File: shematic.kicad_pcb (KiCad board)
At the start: 2 copper layers, 90 x 50.8 mm, 73 parts, among them J1 VIN, J10 SRESU, J11 RESET, J12 Conn_02x03_Odd_Even, J13 Conn_02x03_Odd_Even, J14 Conn_02x03_Odd_Even, J15 X, J16 Y, J17 Z, J2 COOL_ENB, J3 SP/LAS, J4 PROBE, J5 LIM_X, J6 LIM_Y, J7 LIM_Z, J8 ESTOP, J9 FHOLD, U1 4050, U2 MC34063AD, U3 AZ1117-5.0, U4 PC817

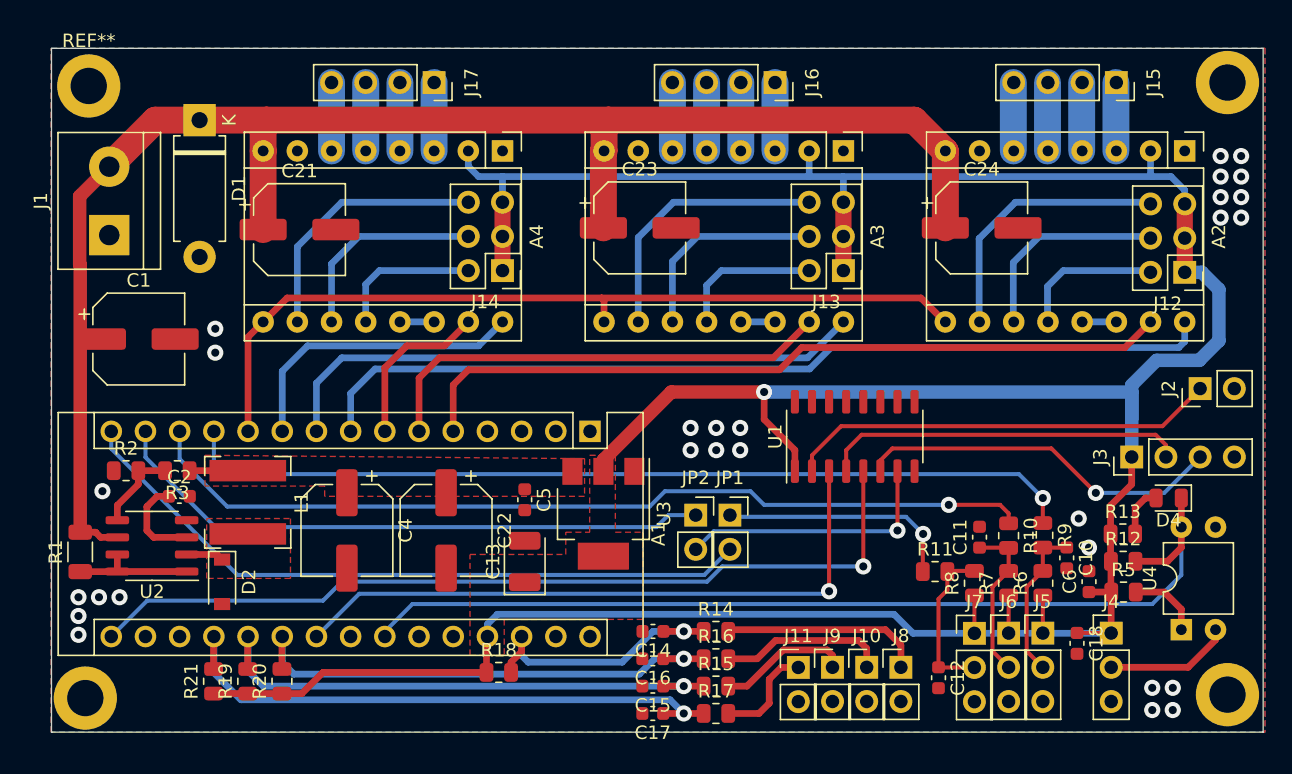
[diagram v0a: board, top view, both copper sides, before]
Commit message: replaced footprints for passive component, edited silkscreens
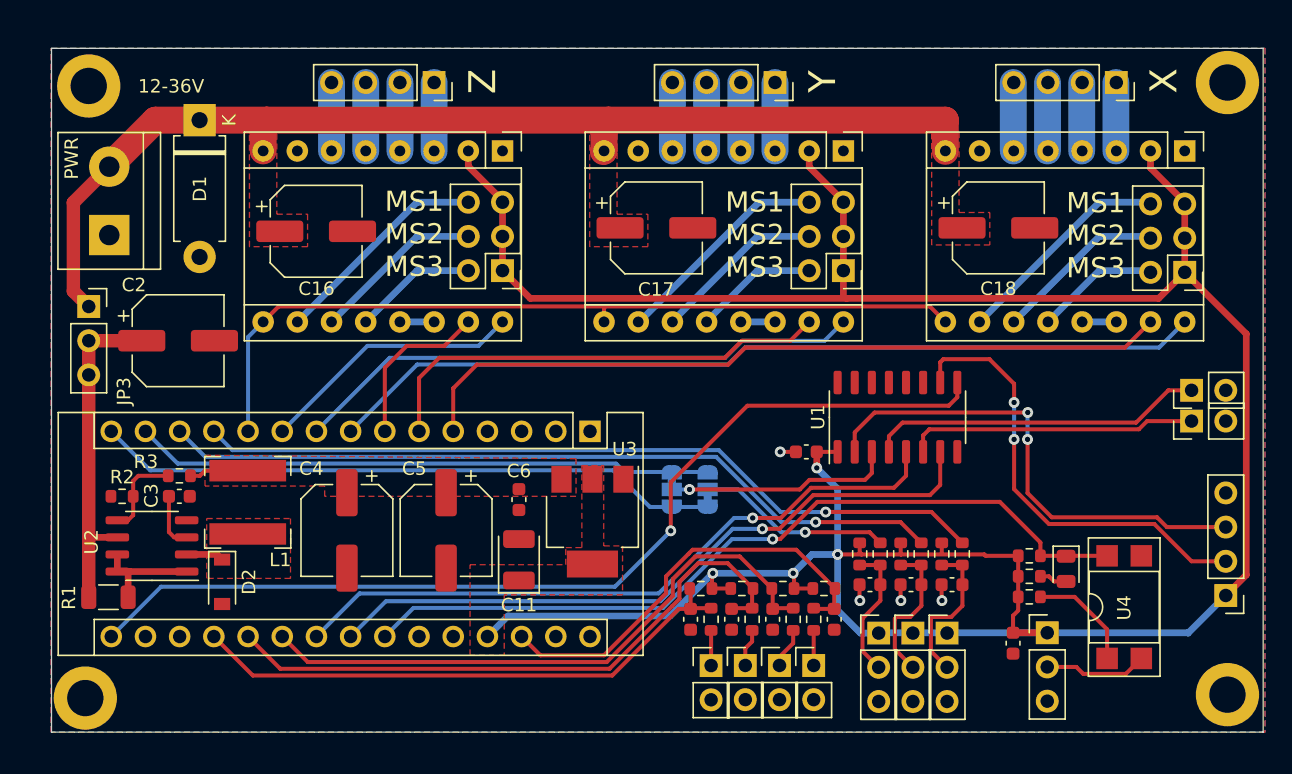
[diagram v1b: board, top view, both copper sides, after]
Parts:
- removed the C18 at (106.2, 73.4)
- added C1: 100n, Capacitor_SMD:C_0603_1608Metric, F.Cu at (86.1, 59.2)
- added J3: COOL_ENB, Connector_PinHeader_2.54mm:PinHeader_1x02_P2.54mm_Vertical, F.Cu at (114.7, 54.6)
- added JP3: EXT_PWR, Connector_PinSocket_2.54mm:PinSocket_1x03_P2.54mm_Vertical, F.Cu at (32.8, 48.4)
- J2: value COOL_ENB -> MIST_ENB
- JP1: value Jumper -> VAR_SP; footprint Connector_PinSocket_2.54mm:PinSocket_1x02_P2.54mm_Vertical -> Jumper:SolderJumper-3_P1.3mm_Bridged12_RoundedPad1.0x1.5mm; moved to B.Cu
- JP2: value Jumper -> LIM_Z; footprint Connector_PinSocket_2.54mm:PinSocket_1x02_P2.54mm_Vertical -> Jumper:SolderJumper-3_P1.3mm_Bridged12_RoundedPad1.0x1.5mm; moved to B.Cu
- R10: renamed from R11; footprint Resistor_SMD:R_0805_2012Metric -> Resistor_SMD:R_0603_1608Metric
- R11: renamed from R12; footprint Resistor_SMD:R_0805_2012Metric -> Resistor_SMD:R_0603_1608Metric
- R12: renamed from R13; footprint Resistor_SMD:R_0805_2012Metric -> Resistor_SMD:R_0603_1608Metric
- R13: renamed from R14; footprint Resistor_SMD:R_0805_2012Metric -> Resistor_SMD:R_0603_1608Metric
- R14: renamed from R15; footprint Resistor_SMD:R_0805_2012Metric -> Resistor_SMD:R_0603_1608Metric
- R15: renamed from R16; footprint Resistor_SMD:R_0805_2012Metric -> Resistor_SMD:R_0603_1608Metric
- R16: renamed from R17; footprint Resistor_SMD:R_0805_2012Metric -> Resistor_SMD:R_0603_1608Metric
- R17: renamed from R18; footprint Resistor_SMD:R_0805_2012Metric -> Resistor_SMD:R_0603_1608Metric
- R18: renamed from R19; footprint Resistor_SMD:R_0805_2012Metric -> Resistor_SMD:R_0603_1608Metric
- R19: renamed from R20; footprint Resistor_SMD:R_0805_2012Metric -> Resistor_SMD:R_0603_1608Metric
- R2, R3: footprint Resistor_SMD:R_0805_2012Metric -> Resistor_SMD:R_0603_1608Metric
- R20: renamed from R21; footprint Resistor_SMD:R_0805_2012Metric -> Resistor_SMD:R_0603_1608Metric
- R4: renamed from R5; footprint Resistor_SMD:R_0805_2012Metric -> Resistor_SMD:R_0603_1608Metric
- R5: renamed from R6; footprint Resistor_SMD:R_0805_2012Metric -> Resistor_SMD:R_0603_1608Metric
- R6: renamed from R7; footprint Resistor_SMD:R_0805_2012Metric -> Resistor_SMD:R_0603_1608Metric
- R7: renamed from R8; footprint Resistor_SMD:R_0805_2012Metric -> Resistor_SMD:R_0603_1608Metric
- R8: renamed from R9; footprint Resistor_SMD:R_0805_2012Metric -> Resistor_SMD:R_0603_1608Metric
- R9: renamed from R10; footprint Resistor_SMD:R_0805_2012Metric -> Resistor_SMD:R_0603_1608Metric
- U4: footprint Package_DIP:DIP-4_W7.62mm -> Package_DIP:DIP-4_W7.62mm_SMDSocket_SmallPads
- moved R19 37.8 mm to (84.3, 69.3), turned to 180 degrees
- moved R18 37.3 mm to (81.3, 69.3), turned to 0 degrees
- moved R20 36.8 mm to (78.2, 69.3), turned to 180 degrees
- moved R17 24.9 mm to (87.4, 69.3)
- moved C12 13.5 mm to (88.1, 71.6), turned to -90 degrees
- moved J4 12.4 mm to (117.2, 69.8), turned to 180 degrees
- moved C14 9.37 mm to (83.6, 71.6), turned to -90 degrees
- moved D3 9.26 mm to (105.4, 67.9), turned to -90 degrees
- moved R7 8.79 mm to (90.0, 66.8), turned to -90 degrees
- moved C8 8.75 mm to (96.9, 69.0), turned to 180 degrees
- moved C10 8.58 mm to (90.8, 69.0), turned to 180 degrees
- moved R6 8.30 mm to (93.1, 66.8), turned to -90 degrees
- moved R5 7.81 mm to (96.1, 66.8), turned to -90 degrees
- moved C13 7.68 mm to (80.5, 71.6), turned to -90 degrees
- moved R12 7.63 mm to (102.6, 68.4)
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- renumbered C12 to C10, C13 to C11, C14 to C12, C15 to C13, C16 to C14, C17 to C15, C21 to C16, C23 to C17, C24 to C18, C1 to C2, C2 to C3, C22 to C5, C5 to C6, C6 to C7, C10 to C8, C11 to C9, D4 to D3, J9 to J10, J10 to J11, J11 to J12, J12 to J13, J13 to J14, J14 to J15, J3 to J4, J4 to J5, J5 to J6, J6 to J7, J7 to J8, J8 to J9, J1 to PWR, J15 to X, J16 to Y, J17 to Z
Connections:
- A1 pad 23: unconnected-(A1-Pad23) -> /MIST_EN
- C2 pad 1: VCC -> Net-(C2-Pad1)
- J4 pad 2: Net-(J3-Pad2) -> Net-(U1-Pad10)
- J4 pad 3: Net-(J3-Pad3) -> Net-(J4-Pad3)
- JP1 pad 1: /LIM_Z -> Net-(A1-Pad14)
- JP1 pad 2: Net-(A1-Pad15) -> /SP_PWM
- JP2 pad 1: Net-(A1-Pad14) -> Net-(A1-Pad15)
- JP2 pad 2: /SP_PWM -> /LIM_Z
- R1 pad 2: VCC -> Net-(C2-Pad1)
- U1 pad 10: (no net) -> Net-(U1-Pad10)
- U1 pad 2: Net-(J2-Pad1) -> Net-(J4-Pad3)
- U1 pad 3: /COOL_EN -> /SP_PWM
- U1 pad 4: Net-(J3-Pad2) -> Net-(J3-Pad1)
- U1 pad 5: /SP_DIR -> /COOL_EN
- U1 pad 6: Net-(J3-Pad3) -> Net-(J2-Pad1)
- U1 pad 7: /SP_PWM -> /MIST_EN
- U1 pad 9: (no net) -> /SP_DIR
- U2 pad 6: VCC -> Net-(C2-Pad1)
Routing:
- net /MIST_EN: track 0.00 -> 50.9 mm, vias 0 -> 1
- net Net-(J4-Pad3): track 0.00 -> 36.7 mm, vias 0 -> 2
- net VCC: track 117.6 -> 82.7 mm
- net Net-(U1-Pad10): track 0.00 -> 33.6 mm, vias 0 -> 2
- net +5V: track 248.4 -> 215.4 mm, vias 1 -> 4
- net Net-(J3-Pad3): track 27.4 -> 0.00 mm, vias 1 -> 0
- net Net-(J3-Pad2): track 27.0 -> 0.00 mm
- net Net-(C2-Pad1): track 0.00 -> 25.2 mm
- net Net-(J3-Pad1): track 0.00 -> 25.1 mm
- net Net-(J9-Pad1): track 15.0 -> 2.60 mm
- net /PROBE: track 72.3 -> 60.1 mm, vias 0 -> 1
- net /ESTOP: track 20.6 -> 32.1 mm, vias 1 -> 0
- net Net-(J2-Pad1): track 32.1 -> 21.6 mm
- net Net-(J11-Pad1): track 12.5 -> 3.02 mm
- net /LIM_Y: track 67.0 -> 58.5 mm
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- added copper zone on F.Cu, net VCC
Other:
- board text added: "12-36V"
- board text added: "MS1 MS2 MS3"
